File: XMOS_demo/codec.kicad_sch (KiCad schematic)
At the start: 24 parts, among them U8 CS4271, Y2 24.576M

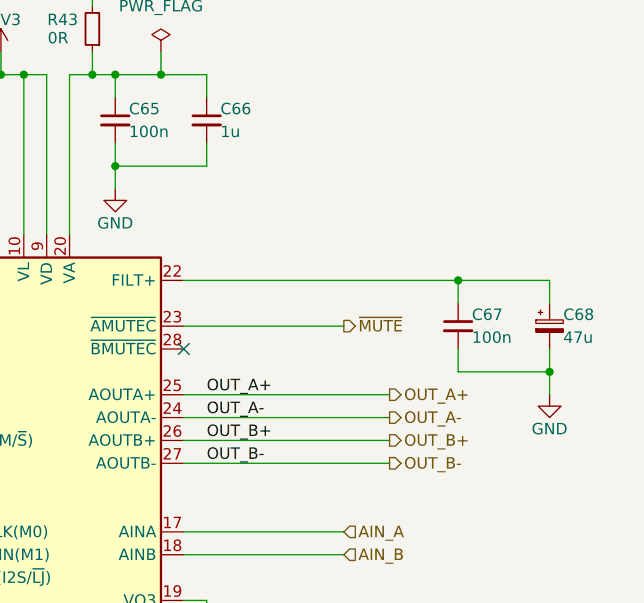
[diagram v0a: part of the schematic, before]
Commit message: Updated sch and pcb with active filter
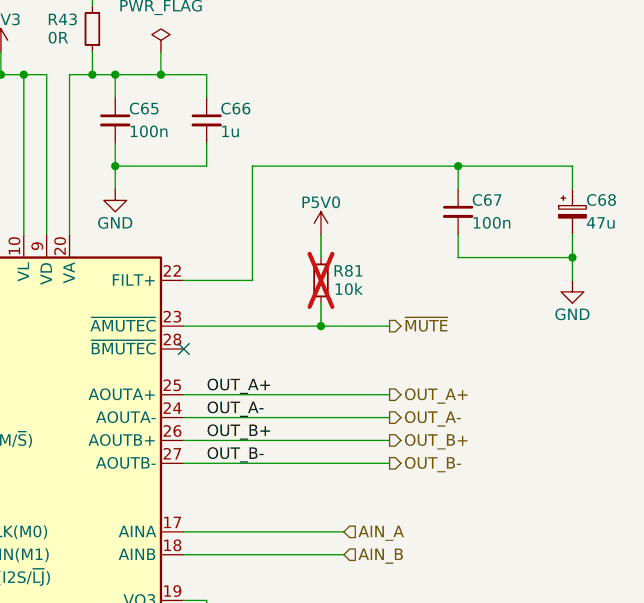
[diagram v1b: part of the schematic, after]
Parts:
- added R81: 10k, Resistor_SMD:R_0603_1608Metric, symbol Device:R_Small
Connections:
- net P5V0: now also R81.1
- net ~{MUTE}: now also R81.2
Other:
- moved on the sheet: C67, C68
